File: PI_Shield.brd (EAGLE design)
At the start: 71.5 x 73 mm, 78 parts, among them J10 T2I, J11 T2I, J12 T2I, J13 DF13-4P-1.25DSA, J14 DF13-4P-1.25DSA, J15 DF13-4P-1.25DSA, J16 T2I5P, J17 USB-MICRO, Q1 220mA/50V/3.5Ω, Q2 220mA/50V/3.5Ω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

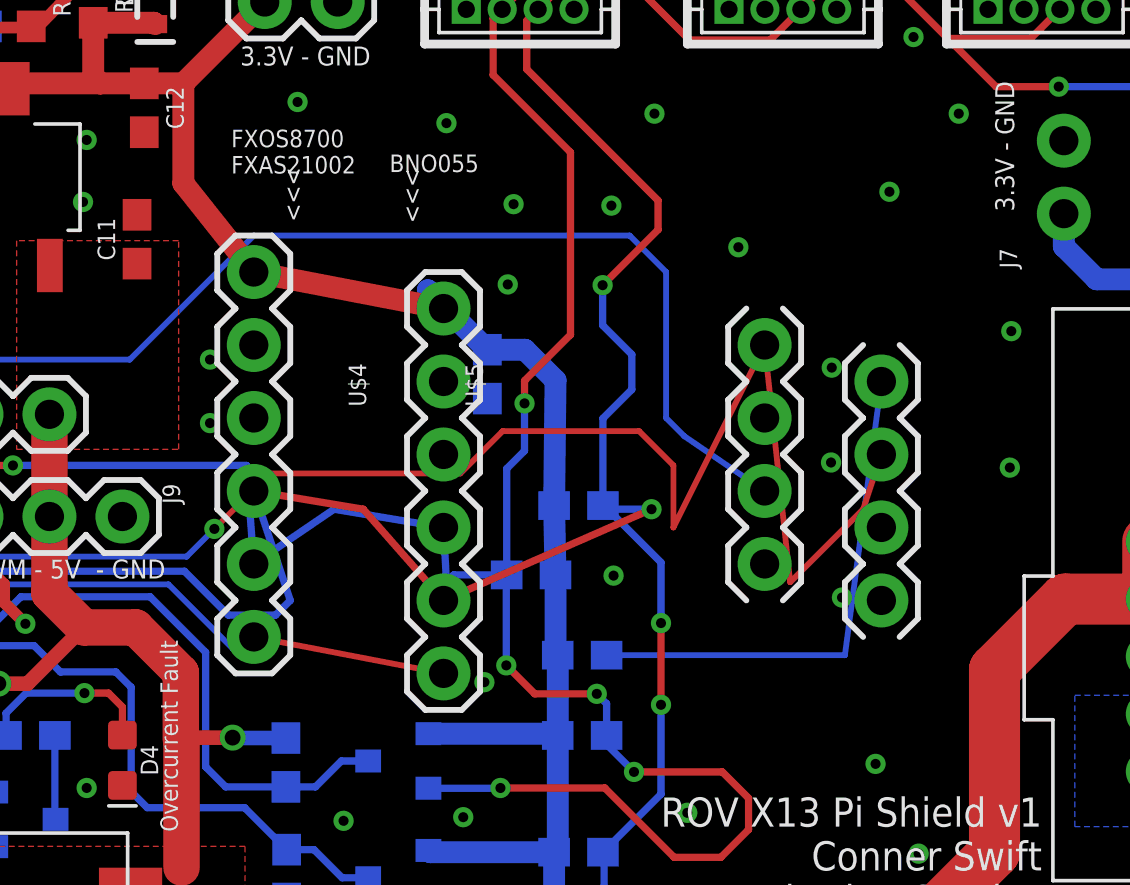
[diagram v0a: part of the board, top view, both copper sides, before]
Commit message: Fixed Swapped IMUs on Schematic
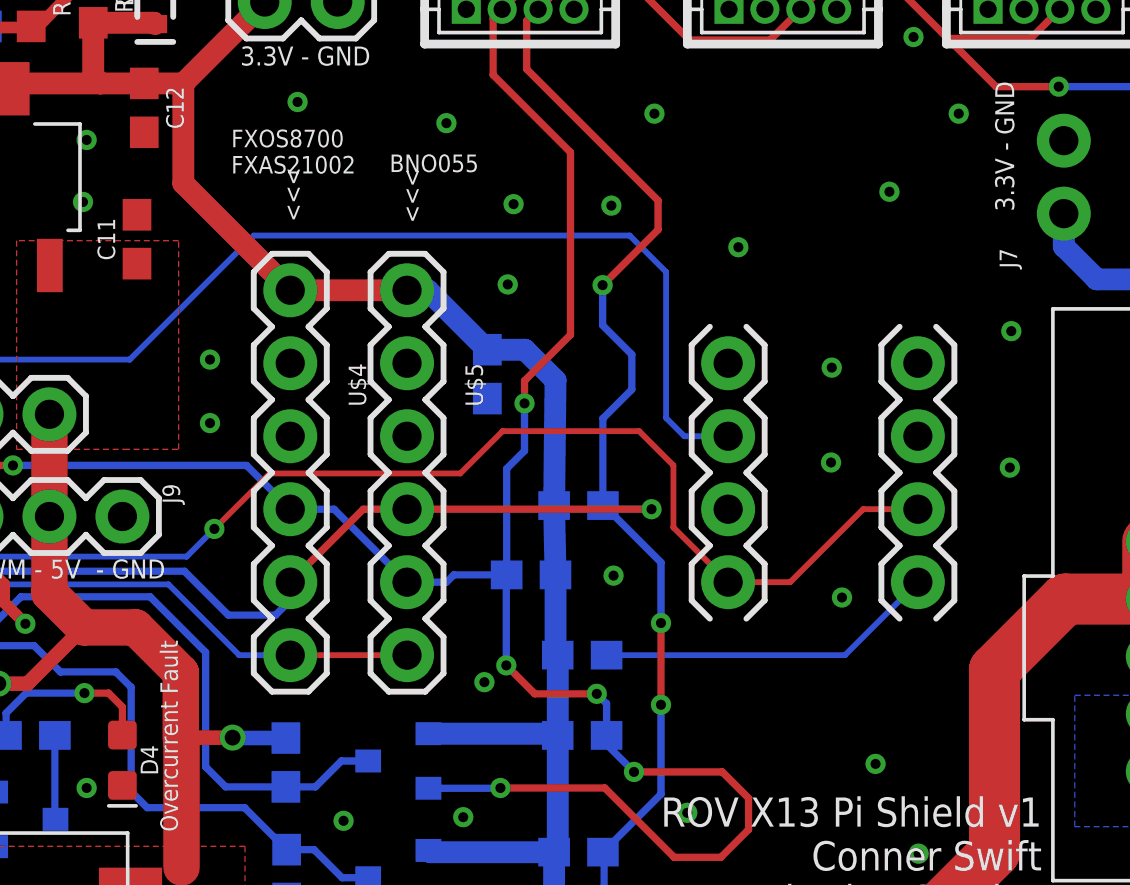
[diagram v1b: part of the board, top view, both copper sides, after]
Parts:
- U$4: value ADAFRUIT-BNO055 -> ADAFRUIT-FXOS8700-FXAS21002; device Adafruit IMUs - BNO055 and FX:ADAFRUIT-BNO055 -> Adafruit IMUs - BNO055 and FX:ADAFRUIT-FXOS8700-FXAS21002
- U$5: value ADAFRUIT-FXOS8700-FXAS21002 -> ADAFRUIT-BNO055; device Adafruit IMUs - BNO055 and FX:ADAFRUIT-FXOS8700-FXAS21002 -> Adafruit IMUs - BNO055 and FX:ADAFRUIT-BNO055
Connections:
- net A_INT: now also U$4.AI1; no longer U$4.INT
- net IMU_INT: now also U$4.GI1, U$5.INT; no longer U$4.PS0, U$5.AI1
- net N$1: now also U$5.ADR; no longer U$5.AI2
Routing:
- net IMU_INT: track 62.3 -> 51.6 mm
- net N$1: track 17.9 -> 11.9 mm
- net SDA: track 133.8 -> 128.1 mm
- net SCL: track 134.1 -> 130.2 mm
- net A_INT: track 61.7 -> 59.8 mm
- net IMU_RESET: track 30.9 -> 29.2 mm
- net 3V3: track 215.6 -> 214.1 mm

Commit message: Updated Parts from Updated X13 Parts Library
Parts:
- U$7: device MCR1101:MCR1101 -> MCR1101:SOIC-16
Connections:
- net !AMP_FAULT: now also U$7.9; no longer U$7.!FAULTB
- net 5V: now also U$7.10, U$7.5, U$7.6, U$7.7, U$7.8; no longer U$7.IP-, U$7.IP-@2, U$7.IP-@3, U$7.IP-@4, U$7.VCC
- net 5V_RAW: now also U$7.1, U$7.2, U$7.3, U$7.4; no longer U$7.IP+, U$7.IP+@2, U$7.IP+@3, U$7.IP+@4
- net AMP_OUT: now also U$7.12; no longer U$7.VOUT
- net GND: now also U$7.11, U$7.14, U$7.15; no longer U$7.GND, U$7.GND@2, U$7.GND@3
- net N$6: now also U$7.13; no longer U$7.VCAP
- net OCD: now also U$7.16; no longer U$7.VOC
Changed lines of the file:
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@@
 <attribute name="VALUE" x="38.5572" y="3.0226" size="1.27" layer="27" align="top-center"/>
 </element>
-<element name="U$7" library="MCR1101" package="MCR1101" value="MCR1101" x="25.146" y="7.62" smashed="yes" rot="R180">
+<element name="U$7" library="MCR1101" package="SOIC-16" value="MCR1101" x="25.146" y="7.62" smashed="yes" rot="R180">
 <attribute name="NAME" x="29.646" y="1.22" size="0.8128" layer="25" rot="R180"/>
 <attribute name="VALUE" x="29.546" y="14.72" size="0.8128" layer="27" rot="R180"/>
@@
 <contactref element="C11" pad="2"/>
 <contactref element="J2" pad="1"/>
-<contactref element="U$7" pad="GND@2"/>
-<contactref element="U$7" pad="GND@3"/>
-<contactref element="U$7" pad="GND"/>
+<contactref element="U$7" pad="14"/>
+<contactref element="U$7" pad="15"/>
+<contactref element="U$7" pad="11"/>
 <contactref element="C10" pad="2"/>
 <via x="7.366" y="5.3086" extent="1-16" drill="0.35"/>
@@
 <contactref element="J12" pad="1"/>
 <contactref element="C11" pad="1"/>
-<contactref element="U$7" pad="IP-"/>
-<contactref element="U$7" pad="IP-@2"/>
-<contactref element="U$7" pad="IP-@4"/>
+<contactref element="U$7" pad="5"/>
+<contactref element="U$7" pad="6"/>
+<contactref element="U$7" pad="8"/>
 <contactref element="R22" pad="1"/>
 <wire x1="17.272" y1="10.834" x2="20.507" y2="10.834" width="0.508" layer="1"/>
@@
 <contactref element="U1" pad="8"/>
 <contactref element="J2" pad="4"/>
-<contactref element="U$7" pad="IP-@3"/>
-<contactref element="U$7" pad="VCC"/>
+<contactref element="U$7" pad="7"/>
+<contactref element="U$7" pad="10"/>
 <contactref element="R23" pad="2"/>
 <contactref element="C10" pad="1"/>
@@
 <vertex x="33.7312" y="7.112"/>
 </polygon>
-<contactref element="U$7" pad="IP+@4"/>
-<contactref element="U$7" pad="IP+@3"/>
-<contactref element="U$7" pad="IP+@2"/>
-<contactref element="U$7" pad="IP+"/>
+<contactref element="U$7" pad="4"/>
+<contactref element="U$7" pad="3"/>
+<contactref element="U$7" pad="2"/>
+<contactref element="U$7" pad="1"/>
 <contactref element="R22" pad="2"/>
 <wire x1="43.307" y1="1.905" x2="43.307" y2="1.8542" width="1.524" layer="1"/>
@@
 <via x="18.6182" y="9.6266" extent="1-16" drill="0.35"/>
 <contactref element="U1" pad="2"/>
-<contactref element="U$7" pad="VOUT"/>
+<contactref element="U$7" pad="12"/>
 <wire x1="18.288" y1="17.0942" x2="17.3736" y2="18.0086" width="0.254" layer="16"/>
 <wire x1="18.6182" y1="9.6266" x2="18.288" y2="9.9568" width="0.254" layer="16"/>
@@
 <wire x1="17.272" y1="7.024" x2="20.507" y2="7.024" width="0.254" layer="1"/>
 <wire x1="20.507" y1="7.024" x2="20.546" y2="6.985" width="0.254" layer="1"/>
-<contactref element="U$7" pad="VCAP"/>
+<contactref element="U$7" pad="13"/>
 </signal>
 <signal name="OCD">
@@
 <wire x1="26.2382" y1="7.024" x2="25.0054" y2="5.7912" width="0.254" layer="16"/>
 <wire x1="25.0054" y1="5.7912" x2="23.8252" y2="5.7912" width="0.254" layer="16"/>
-<contactref element="U$7" pad="VOC"/>
+<contactref element="U$7" pad="16"/>
 <contactref element="R23" pad="1"/>
 <wire x1="20.546" y1="3.175" x2="23.622" y2="3.175" width="0.254" layer="1"/>
@@
 <wire x1="24.9232" y1="13.2588" x2="25.035" y2="13.147" width="0.254" layer="16"/>
 <wire x1="22.8718" y1="13.2588" x2="24.9232" y2="13.2588" width="0.254" layer="16"/>
-<contactref element="U$7" pad="!FAULTB"/>
+<contactref element="U$7" pad="9"/>
 <contactref element="R16" pad="1"/>
 <contactref element="Q5" pad="1"/>

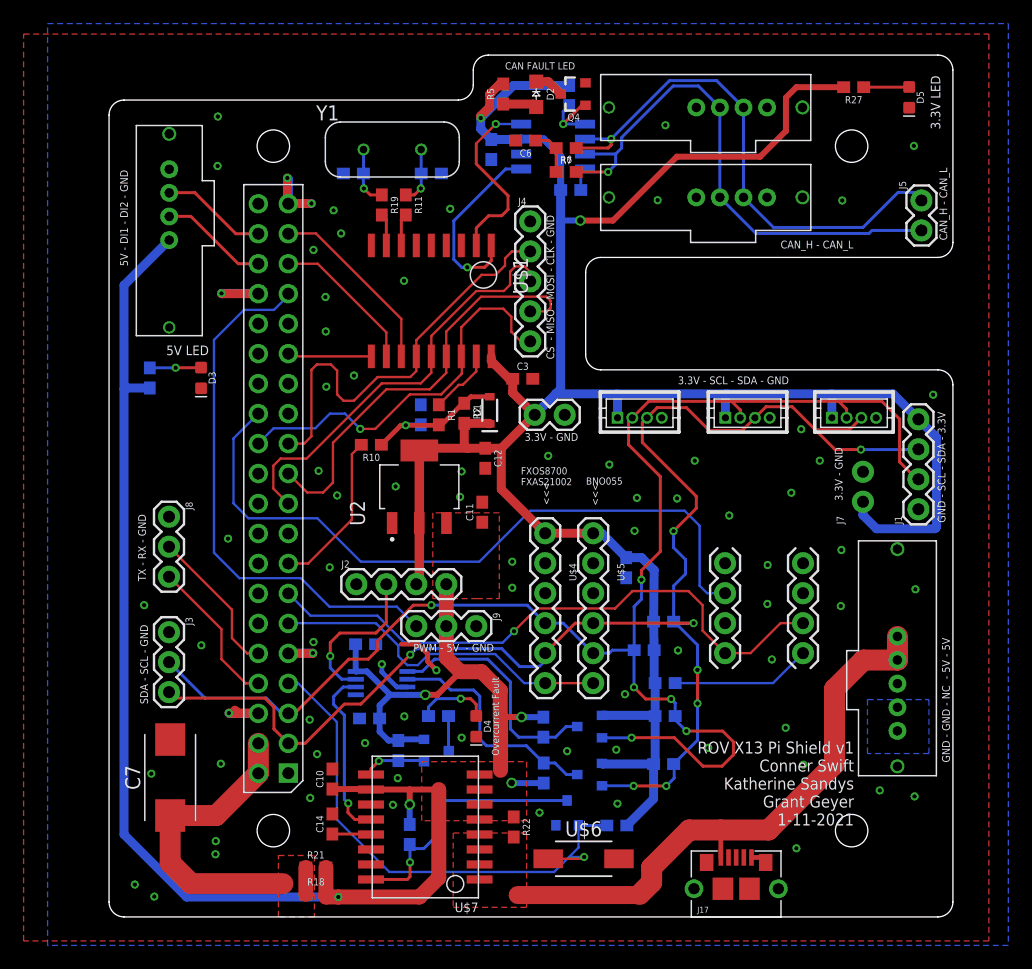
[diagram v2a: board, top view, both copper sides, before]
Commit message: Move USB connector for accessbility and shrink left side for more clearance
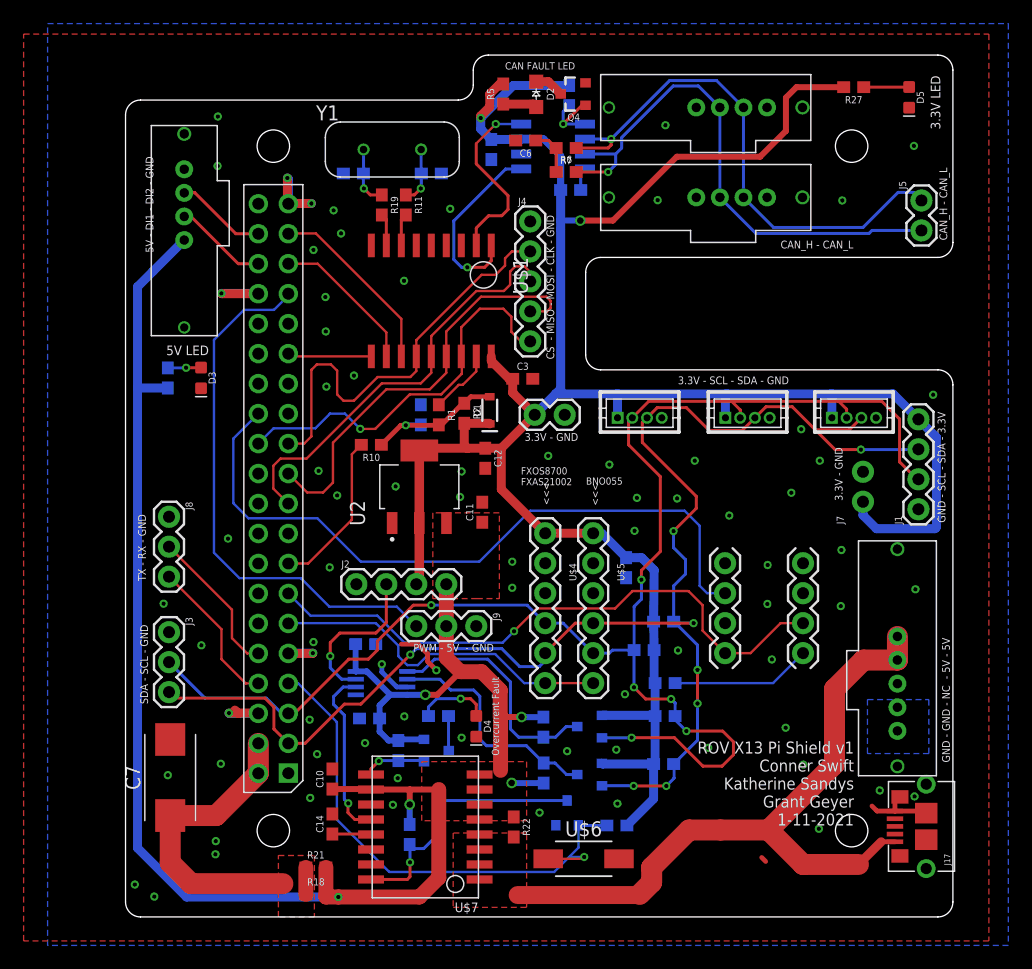
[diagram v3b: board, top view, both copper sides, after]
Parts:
- moved J17 16.9 mm to (67.6, 7.67), turned to 90 degrees
- moved R26 1.52 mm to (3.33, 45.7)
- moved J12 1.27 mm to (7.52, 49.3)
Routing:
- net 5V_RAW: track 49.3 -> 59.7 mm
- net GND: track 33.2 -> 38.5 mm
- net N$9: track 4.35 -> 2.83 mm
- net DI1: track 9.22 -> 7.95 mm
- net DI2: track 9.00 -> 7.73 mm
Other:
- board size 71.5 x 73 mm -> 70.1 x 73 mm

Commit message: Added Resistor Values to Power Indicator LED circuits
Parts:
- R26: value (none) -> 150
- R27: value (none) -> 60
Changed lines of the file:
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@@
 <attribute name="VALUE" x="16.57088125" y="60.63856875" size="1.27245" layer="27"/>
 </element>
-<element name="R26" library="SparkFun-Resistors" library_urn="urn:adsk.eagle:library:532" package="0603" package3d_urn="urn:adsk.eagle:package:39650/1" value="" x="3.3274" y="45.6692" smashed="yes" rot="MR270">
+<element name="R26" library="SparkFun-Resistors" library_urn="urn:adsk.eagle:library:532" package="0603" package3d_urn="urn:adsk.eagle:package:39650/1" value="150" x="3.3274" y="45.6692" smashed="yes" rot="MR270">
 <attribute name="NAME" x="2.5654" y="45.6692" size="0.6096" layer="26" font="vector" ratio="20" rot="MR270" align="bottom-center"/>
 <attribute name="PROD_ID" value=" " x="3.3274" y="45.5168" size="1.778" layer="28" rot="MR270" display="off"/>
 <attribute name="VALUE" x="4.0894" y="45.6692" size="0.6096" layer="28" font="vector" ratio="20" rot="MR270" align="top-center"/>
 </element>
-<element name="R27" library="SparkFun-Resistors" library_urn="urn:adsk.eagle:library:532" package="0603" package3d_urn="urn:adsk.eagle:package:39650/1" value="" x="61.4426" y="70.3072" smashed="yes" rot="R180">
+<element name="R27" library="SparkFun-Resistors" library_urn="urn:adsk.eagle:library:532" package="0603" package3d_urn="urn:adsk.eagle:package:39650/1" value="60" x="61.4426" y="70.3072" smashed="yes" rot="R180">
 <attribute name="NAME" x="61.4426" y="69.5452" size="0.6096" layer="25" font="vector" ratio="20" rot="R180" align="bottom-center"/>
 <attribute name="PROD_ID" value=" " x="61.2902" y="70.3072" size="1.778" layer="27" rot="R180" display="off"/>
